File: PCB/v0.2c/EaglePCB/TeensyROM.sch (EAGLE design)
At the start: 23 parts, among them J1 C64-EXPANSION-PORT, J2 292303-1, J3 J1B1211CCD, J4 4 pin header, U1 Teensy 4.1, U2 74LCV245, U3 74LCV245, U4 74LCV245, U5 74LCV245, U6 74LVC07

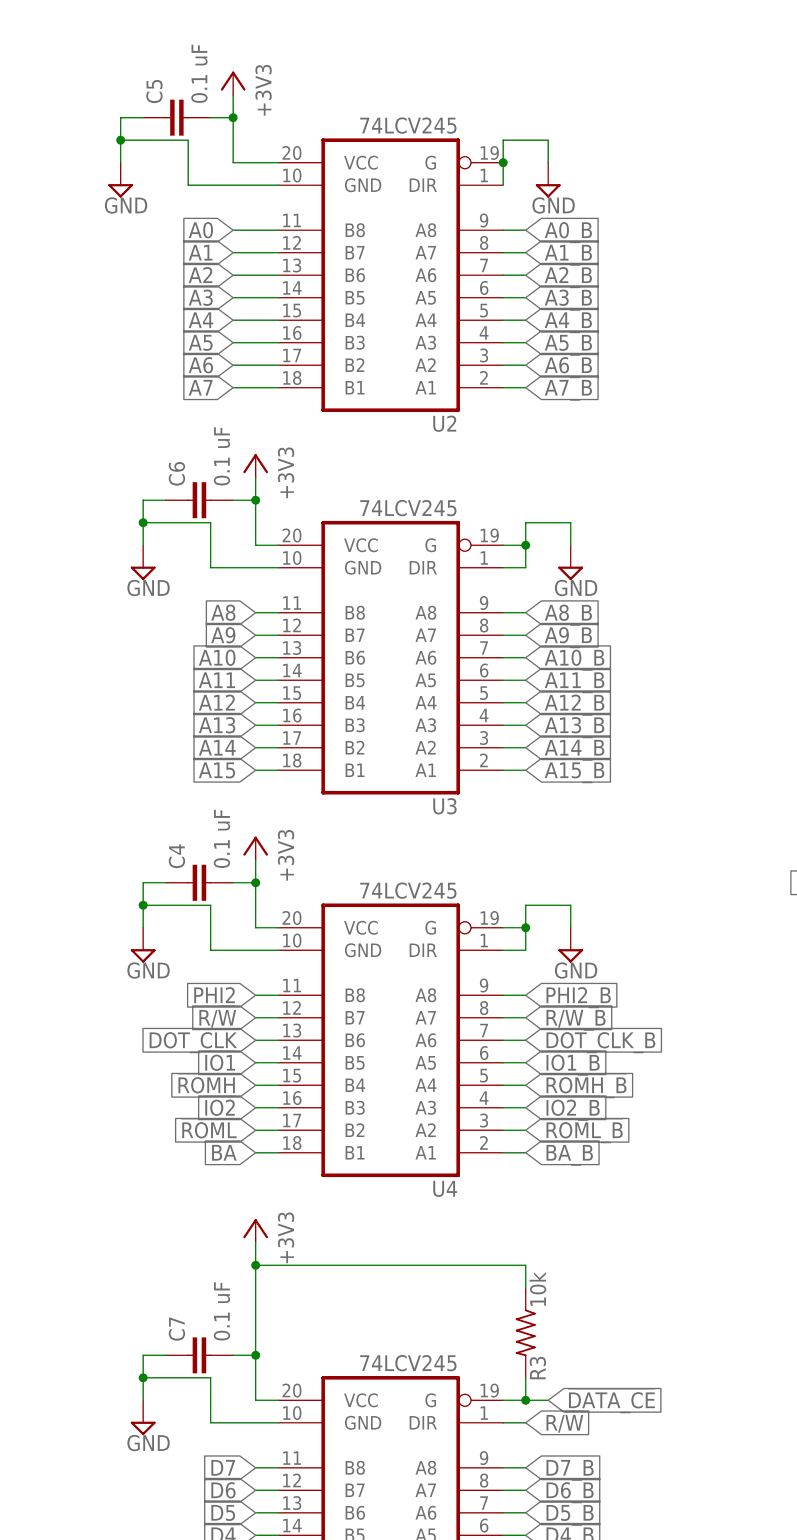
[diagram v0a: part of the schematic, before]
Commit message: Corrected schematic value of 74LVC245, was listed as 74LCV245
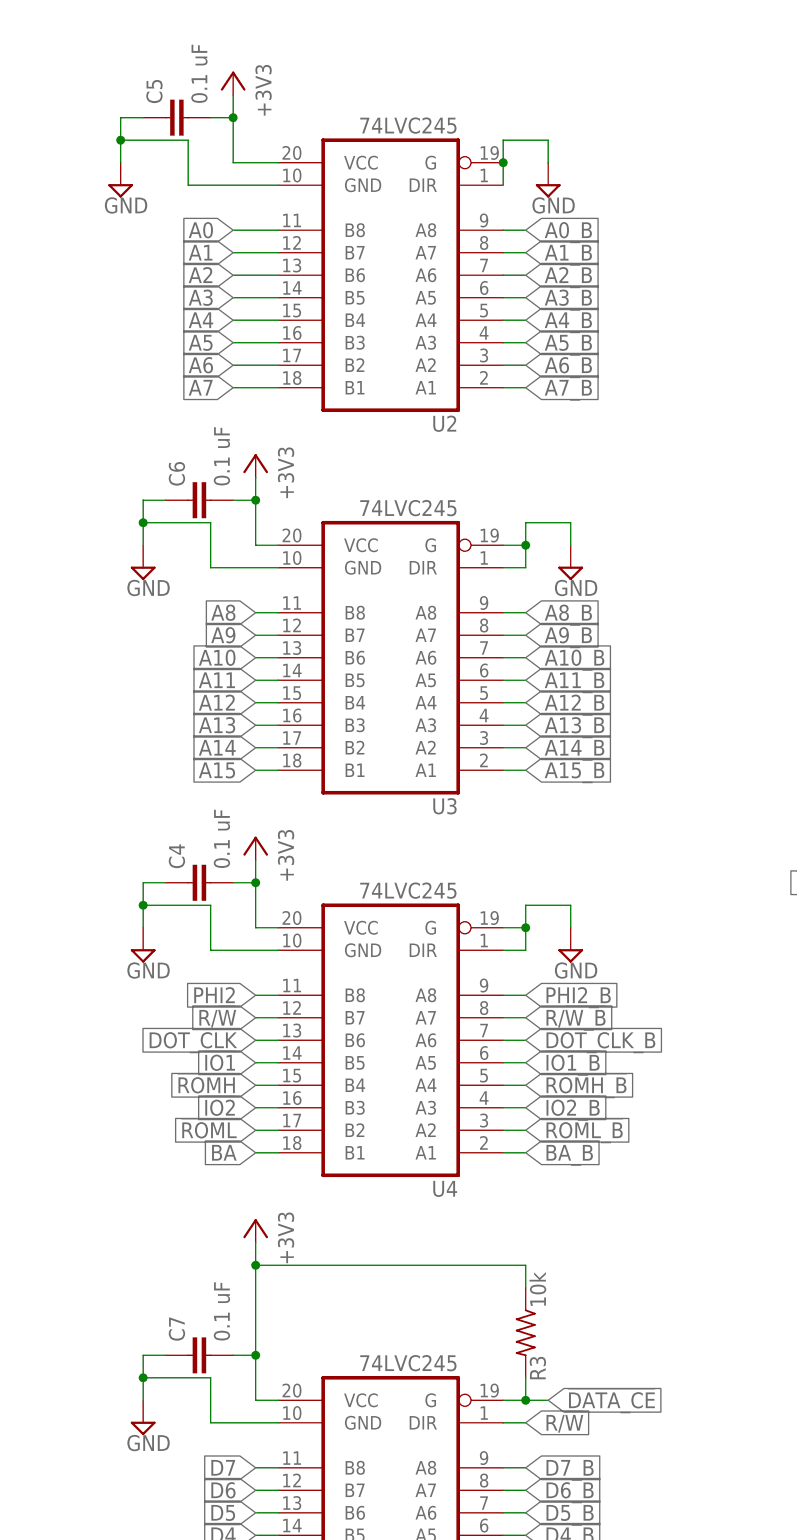
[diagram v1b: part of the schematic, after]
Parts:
- U2, U3, U4, U5: value 74LCV245 -> 74LVC245
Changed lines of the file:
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@@
 <part name="C1" library="TeensyROM" deviceset="CPOL-EU" device="E2-4" value="100uF"/>
 <part name="C2" library="TeensyROM" deviceset="CPOL-EU" device="E2-4" value="100uF"/>
-<part name="U4" library="TeensyROM" deviceset="74*245" device="DW" technology="LS" value="74LCV245"/>
-<part name="U2" library="TeensyROM" deviceset="74*245" device="DW" technology="LS" value="74LCV245"/>
-<part name="U3" library="TeensyROM" deviceset="74*245" device="DW" technology="LS" value="74LCV245"/>
-<part name="U5" library="TeensyROM" deviceset="74*245" device="DW" technology="LS" value="74LCV245"/>
+<part name="U4" library="TeensyROM" deviceset="74*245" device="DW" technology="LS" value="74LVC245"/>
+<part name="U2" library="TeensyROM" deviceset="74*245" device="DW" technology="LS" value="74LVC245"/>
+<part name="U3" library="TeensyROM" deviceset="74*245" device="DW" technology="LS" value="74LVC245"/>
+<part name="U5" library="TeensyROM" deviceset="74*245" device="DW" technology="LS" value="74LVC245"/>
 <part name="SUPPLY4" library="supply2" deviceset="GND" device=""/>
 <part name="SUPPLY5" library="supply2" deviceset="GND" device=""/>
